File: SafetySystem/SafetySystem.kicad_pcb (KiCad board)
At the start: 2 copper layers, 70 x 60 mm, 96 parts, among them J1 Screw_Terminal_01x02, J10 Screw_Terminal_01x02, J2 Screw_Terminal_01x02, J3 Screw_Terminal_01x02, J4 AVR-ISP-10, J5 Screw_Terminal_01x02, J6 Screw_Terminal_01x02, J7 Screw_Terminal_01x02, J8 Screw_Terminal_01x02, J9 Screw_Terminal_01x02, Q1 Q_PMOS_GSD, Q10 Q_NMOS_GSD, Q11 Q_NMOS_GSD, Q12 Q_NMOS_GSD, Q2 Q_PMOS_GSD, Q3 Q_PMOS_GSD, Q4 Q_NMOS_GSD, Q5 Q_NMOS_GSD, Q6 Q_NMOS_GSD, Q7 Q_NMOS_GSD, Q8 Q_NMOS_GSD, Q9 Q_NMOS_GSD, SW2 SW_Push, SW3 SW_Push, SW4 SW_Push, U1 ST1S10PHR, U2 MQ-8, U3 ATmega8A-AU, U4 LTV-817S, U5 LTV-817S, Y1 8Mhz

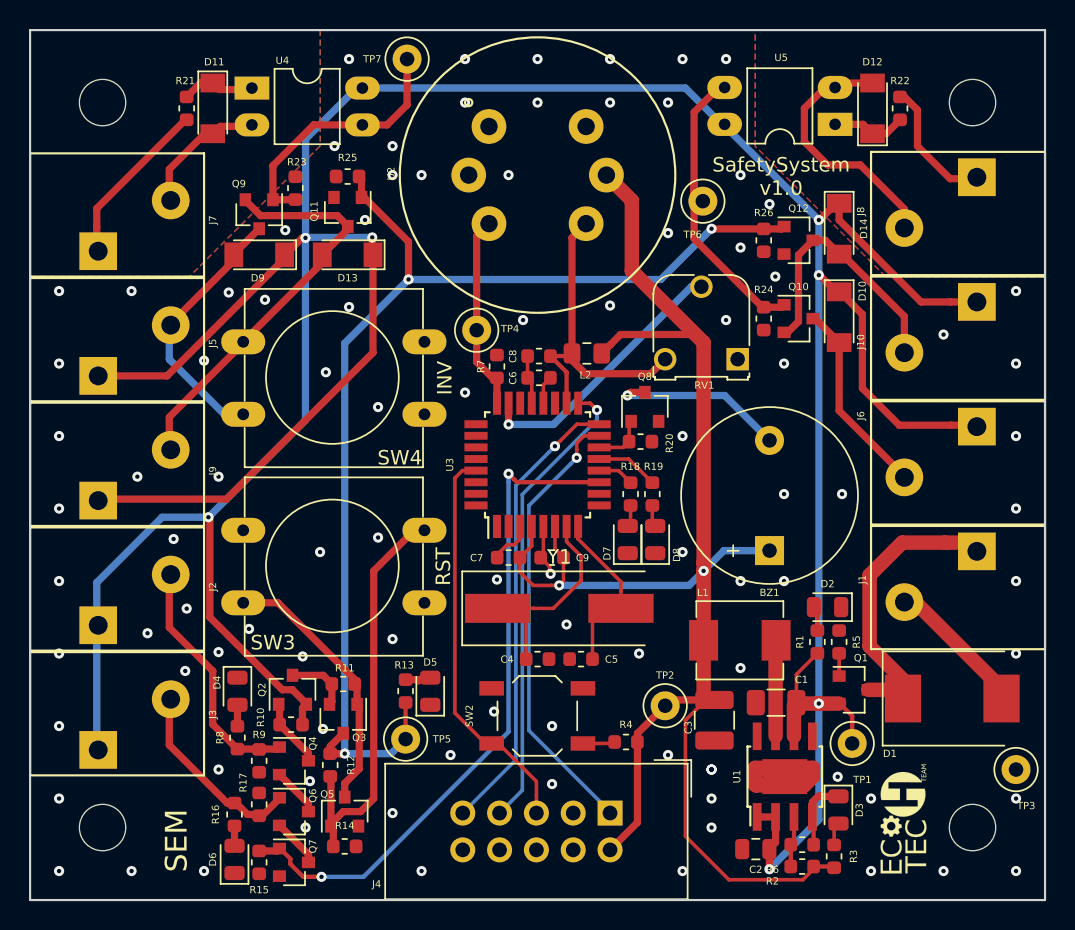
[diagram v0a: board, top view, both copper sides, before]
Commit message: Added version date on silk screen and changed signal tracks width to 0,2.
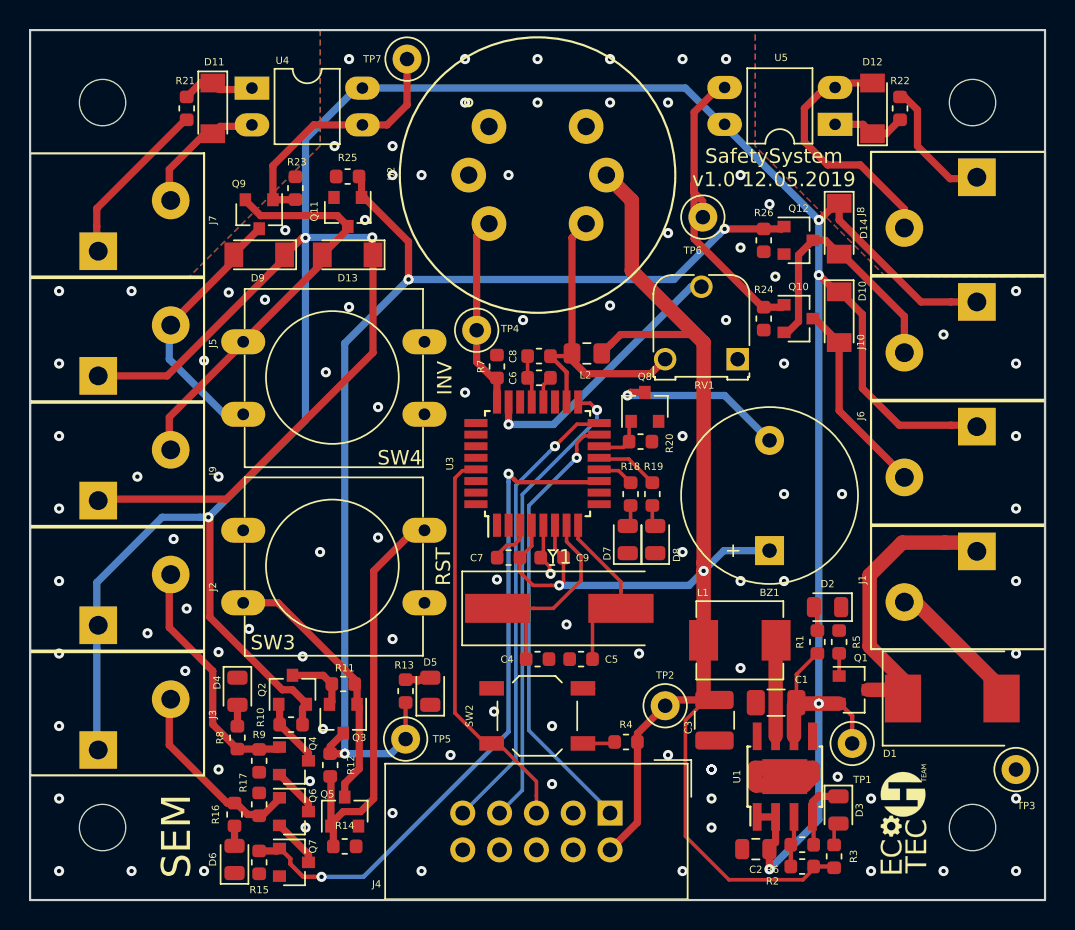
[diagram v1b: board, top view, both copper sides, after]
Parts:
- moved TP6 1.10 mm to (206.4, 62.9)
- moved U3 0.08 mm to (195.0, 79.9)
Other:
- board text added: "SafetySystem v1.0 12.05.2019"
- board text removed: "SafetySystem v1.0"
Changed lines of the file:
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@@
     (thickness 1.6)
     (drawings 8)
-    (tracks 555)
+    (tracks 554)
     (zones 0)
     (modules 96)
@@
     (user_trace_width 2)
     (trace_clearance 0.2)
-    (zone_clearance 0.25)
+    (zone_clearance 0.2)
     (zone_45_only no)
     (trace_min 0.2)
@@
   )
   (module TestPoint:TestPoint_Loop_D1.80mm_Drill1.0mm_Beaded (layer F.Cu)
-    (at 206.4 61.8)
+    (at 206.4 62.9)
     (descr "wire loop with bead as test point, loop diameter 1.8mm, hole diameter 1.0mm")
     (tags "test point wire loop bead")
@@
   )
   (module Package_QFP:TQFP-32_7x7mm_P0.8mm (layer F.Cu)
-    (at 195.000806 79.983504 90)
+    (at 195 79.9 90)
     (descr "32-Lead Plastic Thin Quad Flatpack (PT) - 7x7x1.0 mm Body, 2.00 mm [TQFP] (see Microchip Packaging Specification 00000049BS.pdf)")
     (tags "QFP 0.8")
@@
     )
   )
-  (gr_text "SafetySystem\nv1.0" (at 211.8 60.1) (layer F.SilkS)
+  (gr_text "SafetySystem\nv1.0 12.05.2019" (at 211.3 59.5) (layer F.SilkS)
     (effects (font (size 1 1) (thickness 0.2)))
   )
@@
     (effects (font (size 1 1) (thickness 0.25)))
   )
-  (gr_text SEM (at 170.1 105.9 90) (layer F.SilkS)
-    (effects (font (size 1.5 1.5) (thickness 0.3)))
+  (gr_text SEM (at 170.1 105.6 90) (layer F.SilkS)
+    (effects (font (size 2 2) (thickness 0.3)))
   )
   (gr_line (start 230 110) (end 160 110) (layer Edge.Cuts) (width 0.15))
@@
   (segment (start 184.9 99.9) (end 185.9 98.9) (width 0.5) (layer B.Cu) (net 1))
   (segment (start 181.7 99.9) (end 184.9 99.9) (width 0.5) (layer B.Cu) (net 1))
-  (segment (start 210.6 63.7125) (end 207.0125 63.7125) (width 0.5) (layer F.Cu) (net 1))
-  (via (at 207 63.7) (size 0.7) (drill 0.3) (layers F.Cu B.Cu) (net 1))
-  (segment (start 207.0125 63.7125) (end 207 63.7) (width 0.5) (layer F.Cu) (net 1))
-  (segment (start 186.1 67.2) (end 203.5 67.2) (width 0.5) (layer B.Cu) (net 1))
-  (segment (start 203.5 67.2) (end 206.600001 64.099999) (width 0.5) (layer B.Cu) (net 1))
-  (segment (start 206.600001 64.099999) (end 207 63.7) (width 0.5) (layer B.Cu) (net 1))
+  (segment (start 210.6 63.7125) (end 207.9 63.7125) (width 0.5) (layer F.Cu) (net 1))
+  (segment (start 186.1 67.2) (end 204.4125 67.2) (width 0.5) (layer B.Cu) (net 1))
+  (via (at 207.9 63.7125) (size 0.7) (drill 0.3) (layers F.Cu B.Cu) (net 1))
+  (segment (start 204.4125 67.2) (end 207.550001 64.062499) (width 0.5) (layer B.Cu) (net 1))
+  (segment (start 207.550001 64.062499) (end 207.9 63.7125) (width 0.5) (layer B.Cu) (net 1))
   (segment (start 195.400806 86.196004) (end 195.213306 86.383504) (width 0.25) (layer F.Cu) (net 2))
   (segment (start 195.400806 84.233504) (end 195.400806 86.196004) (width 0.25) (layer F.Cu) (net 2))
@@
   (segment (start 205.6 67.7) (end 196.1 77.2) (width 0.5) (layer B.Cu) (net 65))
   (zone (net 2) (net_name GND) (layer F.Cu) (hatch edge 0.508)
-    (connect_pads (clearance 0.25))
-    (min_thickness 0.25)
-    (fill yes (arc_segments 16) (thermal_gap 0.3) (thermal_bridge_width 0.4))
+    (connect_pads (clearance 0.2))
+    (min_thickness 0.2)
+    (fill yes (arc_segments 16) (thermal_gap 0.2) (thermal_bridge_width 0.4))
     (polygon
       (pts
@@
   )
   (zone (net 2) (net_name GND) (layer B.Cu) (hatch edge 0.508)
-    (connect_pads (clearance 0.25))
-    (min_thickness 0.25)
-    (fill yes (arc_segments 16) (thermal_gap 0.3) (thermal_bridge_width 0.4))
+    (connect_pads (clearance 0.2))
+    (min_thickness 0.2)
+    (fill yes (arc_segments 16) (thermal_gap 0.2) (thermal_bridge_width 0.4))
     (polygon
       (pts
